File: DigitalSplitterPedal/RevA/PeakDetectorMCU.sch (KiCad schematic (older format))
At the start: 14 parts, among them J7 Conn_01x05, U4 STM32F051K8Tx

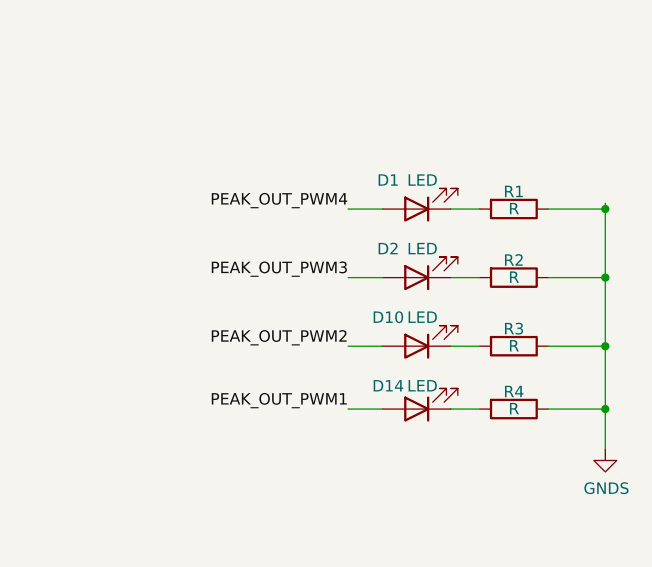
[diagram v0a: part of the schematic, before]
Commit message: HW update
- Completed RevA layout (draft)
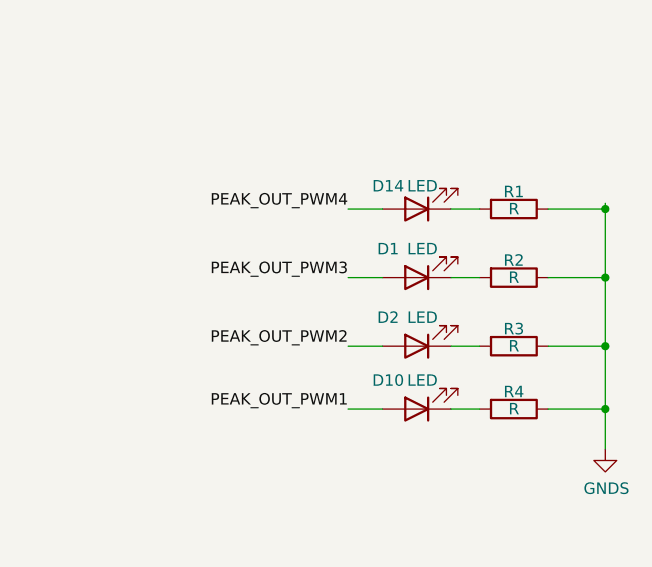
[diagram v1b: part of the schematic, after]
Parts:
- J7: footprint (none) -> Connector_PinHeader_2.54mm:PinHeader_1x05_P2.54mm_Vertical
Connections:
- net PEAK_OUT_PWM1: now also D10.2 (A); no longer D14.2 (A)
- net PEAK_OUT_PWM2: now also D2.2 (A); no longer D10.2 (A)
- net PEAK_OUT_PWM3: now also D1.2 (A); no longer D2.2 (A)
- net PEAK_OUT_PWM4: now also D14.2 (A); no longer D1.2 (A)
- net at D1.1 (K): now also R2.2; no longer R1.2
- net at D2.1 (K): now also R3.2; no longer R2.2
- net at D10.1 (K): now also R4.2; no longer R3.2
- net at D14.1 (K): now also R1.2; no longer R4.2
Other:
- moved on the sheet: D1, D10, D14, D2
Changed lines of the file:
@@
 F 0 "J7" H 5255 6617 50  0000 L CNN
 F 1 "Conn_01x05" H 5255 6526 50  0000 L CNN
-F 2 "" H 5175 6575 50  0001 C CNN
+F 2 "Connector_PinHeader_2.54mm:PinHeader_1x05_P2.54mm_Vertical" H 5175 6575 50  0001 C CNN
 F 3 "~" H 5175 6575 50  0001 C CNN
 	1    5175 6575
@@
 L Device:LED D14
 U 1 1 5F78D251
-P 9600 3175
-F 0 "D14" H 9725 3075 50  0000 C CNN
-F 1 "LED" H 9575 3075 50  0000 C CNN
-F 2 "LED_THT:LED_D5.0mm" H 9600 3175 50  0001 C CNN
-F 3 "~" H 9600 3175 50  0001 C CNN
-	1    9600 3175
+P 9600 2300
+F 0 "D14" H 9725 2200 50  0000 C CNN
+F 1 "LED" H 9575 2200 50  0000 C CNN
+F 2 "LED_THT:LED_D5.0mm" H 9600 2300 50  0001 C CNN
+F 3 "~" H 9600 2300 50  0001 C CNN
+	1    9600 2300
 	-1   0    0    1
 $EndComp
@@
 L Device:LED D10
 U 1 1 5F78B888
-P 9600 2900
-F 0 "D10" H 9725 2775 50  0000 C CNN
-F 1 "LED" H 9575 2775 50  0000 C CNN
-F 2 "LED_THT:LED_D5.0mm" H 9600 2900 50  0001 C CNN
-F 3 "~" H 9600 2900 50  0001 C CNN
-	1    9600 2900
+P 9600 3175
+F 0 "D10" H 9725 3050 50  0000 C CNN
+F 1 "LED" H 9575 3050 50  0000 C CNN
+F 2 "LED_THT:LED_D5.0mm" H 9600 3175 50  0001 C CNN
+F 3 "~" H 9600 3175 50  0001 C CNN
+	1    9600 3175
 	-1   0    0    1
 $EndComp
@@
 L Device:LED D2
 U 1 1 5F78A20E
-P 9600 2600
-F 0 "D2" H 9725 2475 50  0000 C CNN
-F 1 "LED" H 9575 2475 50  0000 C CNN
-F 2 "LED_THT:LED_D5.0mm" H 9600 2600 50  0001 C CNN
-F 3 "~" H 9600 2600 50  0001 C CNN
-	1    9600 2600
+P 9600 2900
+F 0 "D2" H 9725 2775 50  0000 C CNN
+F 1 "LED" H 9575 2775 50  0000 C CNN
+F 2 "LED_THT:LED_D5.0mm" H 9600 2900 50  0001 C CNN
+F 3 "~" H 9600 2900 50  0001 C CNN
+	1    9600 2900
 	-1   0    0    1
 $EndComp
@@
 L Device:LED D1
 U 1 1 5F7849FB
-P 9600 2300
-F 0 "D1" H 9725 2175 50  0000 C CNN
-F 1 "LED" H 9575 2175 50  0000 C CNN
-F 2 "LED_THT:LED_D5.0mm" H 9600 2300 50  0001 C CNN
-F 3 "~" H 9600 2300 50  0001 C CNN
-	1    9600 2300
-	-1   0    0    1
-$EndComp
+P 9600 2600
+F 0 "D1" H 9725 2475 50  0000 C CNN
+F 1 "LED" H 9575 2475 50  0000 C CNN
+F 2 "LED_THT:LED_D5.0mm" H 9600 2600 50  0001 C CNN
+F 3 "~" H 9600 2600 50  0001 C CNN
+	1    9600 2600
+	-1   0    0    1
+$EndComp

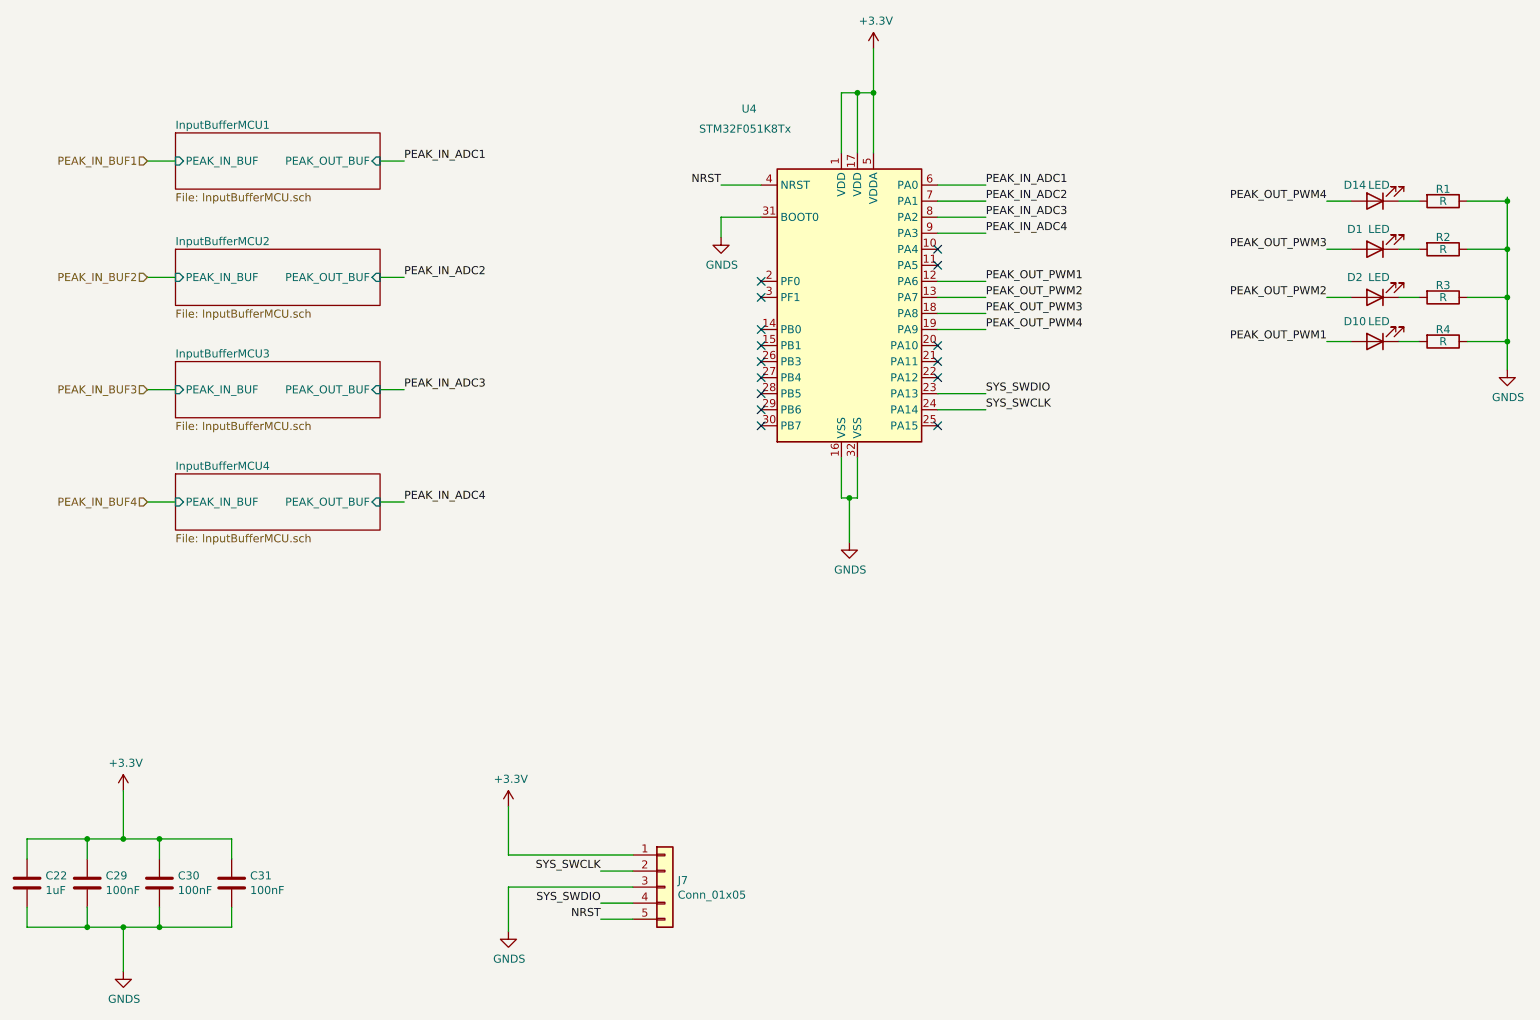
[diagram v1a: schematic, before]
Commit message: updated hw
- add testpoints
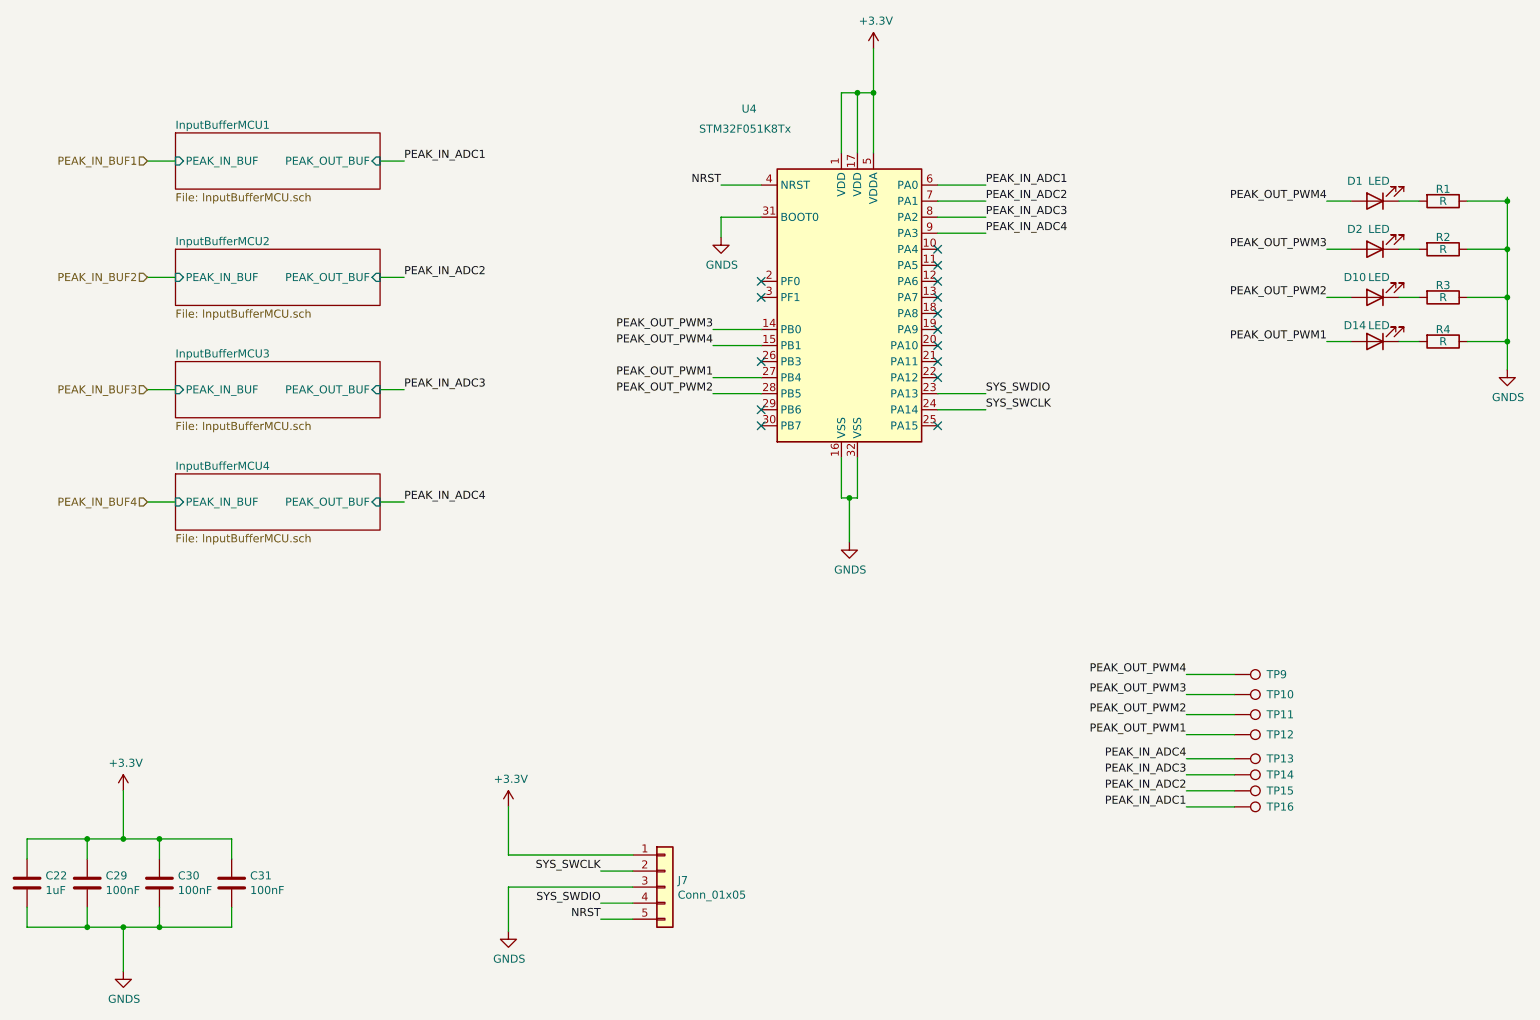
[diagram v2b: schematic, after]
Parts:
- added TP10, TP11, TP12, TP13, TP14, TP15, TP16, TP9: TestPoint, TestPoint:TestPoint_Pad_D1.0mm, symbol Connector:TestPoint
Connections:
- net PEAK_IN_ADC1: now also TP16.1
- net PEAK_IN_ADC2: now also TP15.1
- net PEAK_IN_ADC3: now also TP14.1
- net PEAK_IN_ADC4: now also TP13.1
- net PEAK_OUT_PWM1: now also D14.2 (A), U4.27 (PB4), TP12.1; no longer D10.2 (A), U4.12 (PA6)
- net PEAK_OUT_PWM2: now also D10.2 (A), U4.28 (PB5), TP11.1; no longer D2.2 (A), U4.13 (PA7)
- net PEAK_OUT_PWM3: now also D2.2 (A), U4.14 (PB0), TP10.1; no longer D1.2 (A), U4.18 (PA8)
- net PEAK_OUT_PWM4: now also D1.2 (A), U4.15 (PB1), TP9.1; no longer D14.2 (A), U4.19 (PA9)
- net at D1.1 (K): now also R1.2; no longer R2.2
- net at D14.1 (K): now also R4.2; no longer R1.2
- net at D2.1 (K): now also R2.2; no longer R3.2
- net at D10.1 (K): now also R3.2; no longer R4.2
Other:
- moved on the sheet: D1, D10, D14, D2
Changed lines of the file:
@@
 SYS_SWDIO
 Wire Wire Line
-	6875 2800 7175 2800
-Wire Wire Line
-	6875 2900 7175 2900
-Wire Wire Line
-	6875 3000 7175 3000
-Wire Wire Line
-	6875 3100 7175 3100
+	5775 3400 5475 3400
+Wire Wire Line
+	5775 3500 5475 3500
+Wire Wire Line
+	5775 3100 5475 3100
+Wire Wire Line
+	5775 3200 5475 3200
 NoConn ~ 5775 2800
 NoConn ~ 5775 2900
-NoConn ~ 5775 3100
-NoConn ~ 5775 3200
 NoConn ~ 5775 3300
-NoConn ~ 5775 3400
-NoConn ~ 5775 3500
 NoConn ~ 5775 3600
 NoConn ~ 5775 3700
@@
 Text Label 3550 4175 0    50   ~ 0
 PEAK_IN_ADC4
-Text Label 7175 2800 0    50   ~ 0
+Text Label 5475 3400 2    50   ~ 0
 PEAK_OUT_PWM1
-Text Label 7175 2900 0    50   ~ 0
+Text Label 5475 3500 2    50   ~ 0
 PEAK_OUT_PWM2
-Text Label 7175 3000 0    50   ~ 0
+Text Label 5475 3100 2    50   ~ 0
 PEAK_OUT_PWM3
-Text Label 7175 3100 0    50   ~ 0
+Text Label 5475 3200 2    50   ~ 0
 PEAK_OUT_PWM4
 Wire Wire Line
@@
 L Device:LED D14
 U 1 1 5F78D251
-P 9600 2300
-F 0 "D14" H 9725 2200 50  0000 C CNN
-F 1 "LED" H 9575 2200 50  0000 C CNN
-F 2 "LED_THT:LED_D5.0mm" H 9600 2300 50  0001 C CNN
-F 3 "~" H 9600 2300 50  0001 C CNN
-	1    9600 2300
+P 9600 3175
+F 0 "D14" H 9725 3075 50  0000 C CNN
+F 1 "LED" H 9575 3075 50  0000 C CNN
+F 2 "LED_THT:LED_D5.0mm" H 9600 3175 50  0001 C CNN
+F 3 "~" H 9600 3175 50  0001 C CNN
+	1    9600 3175
 	-1   0    0    1
 $EndComp
@@
 L Device:LED D10
 U 1 1 5F78B888
-P 9600 3175
-F 0 "D10" H 9725 3050 50  0000 C CNN
-F 1 "LED" H 9575 3050 50  0000 C CNN
-F 2 "LED_THT:LED_D5.0mm" H 9600 3175 50  0001 C CNN
-F 3 "~" H 9600 3175 50  0001 C CNN
-	1    9600 3175
+P 9600 2900
+F 0 "D10" H 9725 2775 50  0000 C CNN
+F 1 "LED" H 9575 2775 50  0000 C CNN
+F 2 "LED_THT:LED_D5.0mm" H 9600 2900 50  0001 C CNN
+F 3 "~" H 9600 2900 50  0001 C CNN
+	1    9600 2900
 	-1   0    0    1
 $EndComp
@@
 L Device:LED D2
 U 1 1 5F78A20E
-P 9600 2900
-F 0 "D2" H 9725 2775 50  0000 C CNN
-F 1 "LED" H 9575 2775 50  0000 C CNN
-F 2 "LED_THT:LED_D5.0mm" H 9600 2900 50  0001 C CNN
-F 3 "~" H 9600 2900 50  0001 C CNN
-	1    9600 2900
+P 9600 2600
+F 0 "D2" H 9725 2475 50  0000 C CNN
+F 1 "LED" H 9575 2475 50  0000 C CNN
+F 2 "LED_THT:LED_D5.0mm" H 9600 2600 50  0001 C CNN
+F 3 "~" H 9600 2600 50  0001 C CNN
+	1    9600 2600
 	-1   0    0    1
 $EndComp
@@
 L Device:LED D1
 U 1 1 5F7849FB
-P 9600 2600
-F 0 "D1" H 9725 2475 50  0000 C CNN
-F 1 "LED" H 9575 2475 50  0000 C CNN
-F 2 "LED_THT:LED_D5.0mm" H 9600 2600 50  0001 C CNN
-F 3 "~" H 9600 2600 50  0001 C CNN
-	1    9600 2600
+P 9600 2300
+F 0 "D1" H 9725 2175 50  0000 C CNN
+F 1 "LED" H 9575 2175 50  0000 C CNN
+F 2 "LED_THT:LED_D5.0mm" H 9600 2300 50  0001 C CNN
+F 3 "~" H 9600 2300 50  0001 C CNN
+	1    9600 2300
 	-1   0    0    1
 $EndComp
@@
 F3 "PEAK_OUT_BUF" I R 3400 2050 50
 $EndSheet
+NoConn ~ 6875 2800
+NoConn ~ 6875 2900
+NoConn ~ 6875 3000
+NoConn ~ 6875 3100
+Text Label 8425 5250 2    50   ~ 0
+PEAK_OUT_PWM4
+Text Label 8425 5375 2    50   ~ 0
+PEAK_OUT_PWM3
+Text Label 8425 5500 2    50   ~ 0
+PEAK_OUT_PWM2
+Text Label 8425 5625 2    50   ~ 0
+PEAK_OUT_PWM1
+$Comp
+L Connector:TestPoint TP?
+U 1 1 5F6E6675
+P 8725 5250
+AR Path="/5F6CB11D/5F6E6675" Ref="TP?"  Part="1"
+AR Path="/5F6F05C2/5F6E6675" Ref="TP?"  Part="1"
+AR Path="/5F6F456E/5F6E6675" Ref="TP?"  Part="1"
+AR Path="/5F6F8B66/5F6E6675" Ref="TP?"  Part="1"
+AR Path="/5F6CB23D/5F6E6675" Ref="TP9"  Part="1"
+F 0 "TP9" V 8725 5450 50  0000 L CNN
+F 1 "TestPoint" V 8500 5200 50  0001 L CNN
+F 2 "TestPoint:TestPoint_Pad_D1.0mm" H 8925 5250 50  0001 C CNN
+F 3 "~" H 8925 5250 50  0001 C CNN
+	1    8725 5250
+	0    1    1    0
+$EndComp
+Wire Wire Line
+	8425 5250 8725 5250
+$Comp
+L Connector:TestPoint TP?
+U 1 1 5F6ECAE6
+P 8725 5375
+AR Path="/5F6CB11D/5F6ECAE6" Ref="TP?"  Part="1"
+AR Path="/5F6F05C2/5F6ECAE6" Ref="TP?"  Part="1"
+AR Path="/5F6F456E/5F6ECAE6" Ref="TP?"  Part="1"
+AR Path="/5F6F8B66/5F6ECAE6" Ref="TP?"  Part="1"
+AR Path="/5F6CB23D/5F6ECAE6" Ref="TP10"  Part="1"
+F 0 "TP10" V 8725 5575 50  0000 L CNN
+F 1 "TestPoint" V 8500 5325 50  0001 L CNN
+F 2 "TestPoint:TestPoint_Pad_D1.0mm" H 8925 5375 50  0001 C CNN
+F 3 "~" H 8925 5375 50  0001 C CNN
+	1    8725 5375
+	0    1    1    0
+$EndComp
+Wire Wire Line
+	8425 5375 8725 5375
+$Comp
+L Connector:TestPoint TP?
+U 1 1 5F6F5F7C
+P 8725 5500
+AR Path="/5F6CB11D/5F6F5F7C" Ref="TP?"  Part="1"
+AR Path="/5F6F05C2/5F6F5F7C" Ref="TP?"  Part="1"
+AR Path="/5F6F456E/5F6F5F7C" Ref="TP?"  Part="1"
+AR Path="/5F6F8B66/5F6F5F7C" Ref="TP?"  Part="1"
+AR Path="/5F6CB23D/5F6F5F7C" Ref="TP11"  Part="1"
+F 0 "TP11" V 8725 5700 50  0000 L CNN
+F 1 "TestPoint" V 8500 5450 50  0001 L CNN
+F 2 "TestPoint:TestPoint_Pad_D1.0mm" H 8925 5500 50  0001 C CNN
+F 3 "~" H 8925 5500 50  0001 C CNN
+	1    8725 5500
+	0    1    1    0
+$EndComp
+Wire Wire Line
+	8425 5500 8725 5500
+$Comp
+L Connector:TestPoint TP?
+U 1 1 5F6F8049
+P 8725 5625
+AR Path="/5F6CB11D/5F6F8049" Ref="TP?"  Part="1"
+AR Path="/5F6F05C2/5F6F8049" Ref="TP?"  Part="1"
+AR Path="/5F6F456E/5F6F8049" Ref="TP?"  Part="1"
+AR Path="/5F6F8B66/5F6F8049" Ref="TP?"  Part="1"
+AR Path="/5F6CB23D/5F6F8049" Ref="TP12"  Part="1"
+F 0 "TP12" V 8725 5825 50  0000 L CNN
+F 1 "TestPoint" V 8500 5575 50  0001 L CNN
+F 2 "TestPoint:TestPoint_Pad_D1.0mm" H 8925 5625 50  0001 C CNN
+F 3 "~" H 8925 5625 50  0001 C CNN
+	1    8725 5625
+	0    1    1    0
+$EndComp
+Wire Wire Line
+	8425 5625 8725 5625
+Wire Wire Line
+	8725 6075 8425 6075
+Text Label 8425 6075 2    50   ~ 0
+PEAK_IN_ADC1
+Wire Wire Line
+	8725 5975 8425 5975
+Text Label 8425 5975 2    50   ~ 0
+PEAK_IN_ADC2
+Wire Wire Line
+	8725 5875 8425 5875
+Text Label 8425 5875 2    50   ~ 0
+PEAK_IN_ADC3
+Wire Wire Line
+	8725 5775 8425 5775
+Text Label 8425 5775 2    50   ~ 0
+PEAK_IN_ADC4
+$Comp
+L Connector:TestPoint TP?
+U 1 1 5F6FC372
+P 8725 5775
+AR Path="/5F6CB11D/5F6FC372" Ref="TP?"  Part="1"
+AR Path="/5F6F05C2/5F6FC372" Ref="TP?"  Part="1"
+AR Path="/5F6F456E/5F6FC372" Ref="TP?"  Part="1"
+AR Path="/5F6F8B66/5F6FC372" Ref="TP?"  Part="1"
+AR Path="/5F6CB23D/5F6FC372" Ref="TP13"  Part="1"
+F 0 "TP13" V 8725 5975 50  0000 L CNN
+F 1 "TestPoint" V 8500 5725 50  0001 L CNN
+F 2 "TestPoint:TestPoint_Pad_D1.0mm" H 8925 5775 50  0001 C CNN
+F 3 "~" H 8925 5775 50  0001 C CNN
+	1    8725 5775
+	0    1    1    0
+$EndComp
+$Comp
+L Connector:TestPoint TP?
+U 1 1 5F6FC884
+P 8725 5875
+AR Path="/5F6CB11D/5F6FC884" Ref="TP?"  Part="1"
+AR Path="/5F6F05C2/5F6FC884" Ref="TP?"  Part="1"
+AR Path="/5F6F456E/5F6FC884" Ref="TP?"  Part="1"
+AR Path="/5F6F8B66/5F6FC884" Ref="TP?"  Part="1"
+AR Path="/5F6CB23D/5F6FC884" Ref="TP14"  Part="1"
+F 0 "TP14" V 8725 6075 50  0000 L CNN
+F 1 "TestPoint" V 8500 5825 50  0001 L CNN
+F 2 "TestPoint:TestPoint_Pad_D1.0mm" H 8925 5875 50  0001 C CNN
+F 3 "~" H 8925 5875 50  0001 C CNN
+	1    8725 5875
+	0    1    1    0
+$EndComp
+$Comp
+L Connector:TestPoint TP?
+U 1 1 5F6FD804
+P 8725 5975
+AR Path="/5F6CB11D/5F6FD804" Ref="TP?"  Part="1"
+AR Path="/5F6F05C2/5F6FD804" Ref="TP?"  Part="1"
+AR Path="/5F6F456E/5F6FD804" Ref="TP?"  Part="1"
+AR Path="/5F6F8B66/5F6FD804" Ref="TP?"  Part="1"
+AR Path="/5F6CB23D/5F6FD804" Ref="TP15"  Part="1"
+F 0 "TP15" V 8725 6175 50  0000 L CNN
+F 1 "TestPoint" V 8500 5925 50  0001 L CNN
+F 2 "TestPoint:TestPoint_Pad_D1.0mm" H 8925 5975 50  0001 C CNN
+F 3 "~" H 8925 5975 50  0001 C CNN
+	1    8725 5975
+	0    1    1    0
+$EndComp
+$Comp
+L Connector:TestPoint TP?
+U 1 1 5F6FDB02
+P 8725 6075
+AR Path="/5F6CB11D/5F6FDB02" Ref="TP?"  Part="1"
+AR Path="/5F6F05C2/5F6FDB02" Ref="TP?"  Part="1"
+AR Path="/5F6F456E/5F6FDB02" Ref="TP?"  Part="1"
+AR Path="/5F6F8B66/5F6FDB02" Ref="TP?"  Part="1"
+AR Path="/5F6CB23D/5F6FDB02" Ref="TP16"  Part="1"
+F 0 "TP16" V 8725 6275 50  0000 L CNN
+F 1 "TestPoint" V 8500 6025 50  0001 L CNN
+F 2 "TestPoint:TestPoint_Pad_D1.0mm" H 8925 6075 50  0001 C CNN
+F 3 "~" H 8925 6075 50  0001 C CNN
+	1    8725 6075
+	0    1    1    0
+$EndComp
 $EndSCHEMATC
